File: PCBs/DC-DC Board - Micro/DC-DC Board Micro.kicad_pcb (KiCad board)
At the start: 2 copper layers, 58.4 x 36.8 mm, 56 parts, among them J1 Conn_01x01, J2 Conn_01x01, J3 Conn_01x02, J4 Conn_01x03, J5 Conn_01x01, J6 Conn_01x01, J7 USB_B_Mini, J8 Conn_02x05_Odd_Even, Q1 Q_NMOS_GDS, SW1 SW_Push, U1 ACS711, U2 DBQ0135V2, U3 TLV733P, U4 ATSAMD21E16L-MFT, Y1 32.7680kHz

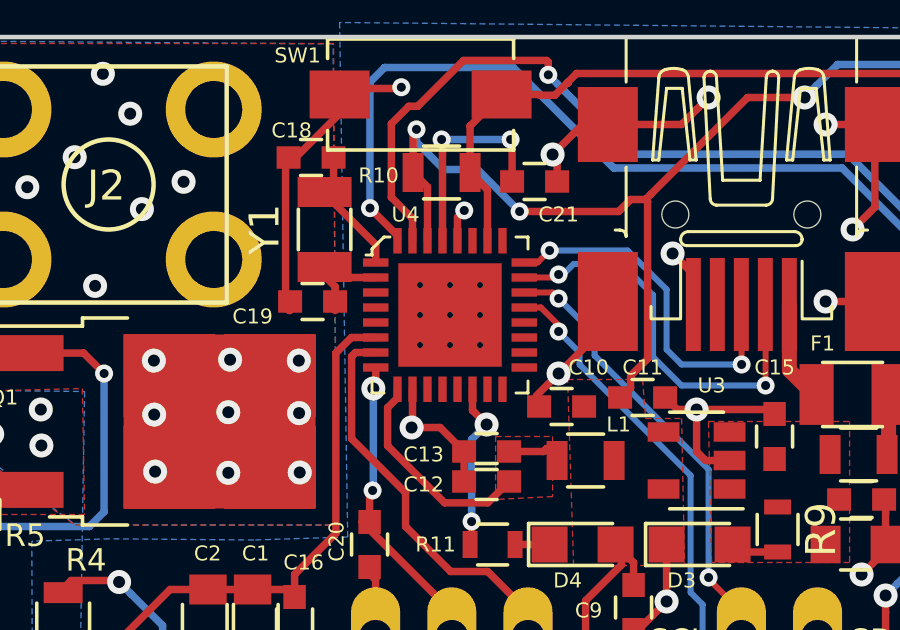
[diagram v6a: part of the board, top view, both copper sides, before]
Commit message: Minor Updates
Trying to sneak these Power PCBs through PCBWay, they caught me on a few 0.2mm drills so I made em 0.3. We'll see if my 0.2mm clearance passes their 8mil clearance (0.2035mm)
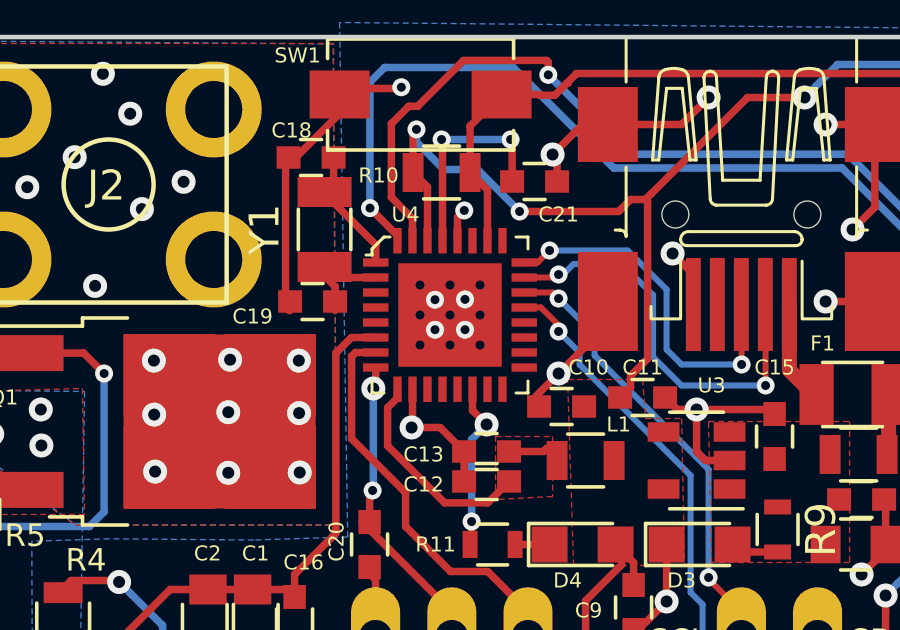
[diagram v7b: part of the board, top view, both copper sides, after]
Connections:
- U4 pad 33: (no net) -> GND
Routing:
- net GND: vias 35 -> 39
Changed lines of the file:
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@@
     (thickness 1.6)
     (drawings 24)
-    (tracks 512)
+    (tracks 516)
     (zones 0)
     (modules 56)
@@
     (last_trace_width 0.25)
     (trace_clearance 0.2)
-    (zone_clearance 0.25)
+    (zone_clearance 0.21)
     (zone_45_only no)
     (trace_min 0.2)
@@
     (uvia_drill 0.1)
     (uvias_allowed no)
-    (uvia_min_size 0.2)
+    (uvia_min_size 0.3)
     (uvia_min_drill 0.1)
     (pcb_text_width 0.3)
@@
     (visible_elements 7FFFFFFF)
     (pcbplotparams
-      (layerselection 0x010fc_ffffffff)
-      (usegerberextensions false)
+      (layerselection 0x010f0_ffffffff)
+      (usegerberextensions true)
       (usegerberattributes false)
       (usegerberadvancedattributes false)
@@
       (padsonsilk false)
       (subtractmaskfromsilk false)
-      (outputformat 4)
-      (mirror true)
+      (outputformat 1)
+      (mirror false)
       (drillshape 0)
       (scaleselection 1)
-      (outputdirectory ""))
+      (outputdirectory "Gerbers/"))
   )
   (net 0 "")
@@
     (pad 1 smd rect (at -2.995 -2.2 270) (size 0.28 0.85) (layers F.Cu F.Paste F.Mask)
       (net 21 "Net-(C18-Pad1)") (solder_mask_margin 0.07))
-    (pad 33 thru_hole circle (at -1.52 0.55 270) (size 0.2 0.2) (drill 0.2) (layers *.Cu *.Mask)
+    (pad 33 thru_hole circle (at -1.52 0.55 270) (size 0.3 0.3) (drill 0.3) (layers *.Cu *.Mask)
       (solder_mask_margin 0.1))
-    (pad 33 thru_hole circle (at -1.52 -0.45 270) (size 0.2 0.2) (drill 0.2) (layers *.Cu *.Mask)
+    (pad 33 thru_hole circle (at -1.52 -0.45 270) (size 0.3 0.3) (drill 0.3) (layers *.Cu *.Mask)
       (solder_mask_margin 0.1))
-    (pad 33 thru_hole circle (at -1.52 -1.45 270) (size 0.2 0.2) (drill 0.2) (layers *.Cu *.Mask)
+    (pad 33 thru_hole circle (at -1.52 -1.45 270) (size 0.3 0.3) (drill 0.3) (layers *.Cu *.Mask)
       (solder_mask_margin 0.1))
-    (pad 33 thru_hole circle (at -0.52 0.55 270) (size 0.2 0.2) (drill 0.2) (layers *.Cu *.Mask)
+    (pad 33 thru_hole circle (at -0.52 0.55 270) (size 0.3 0.3) (drill 0.3) (layers *.Cu *.Mask)
       (solder_mask_margin 0.1))
-    (pad 33 thru_hole circle (at -0.52 -0.450001 270) (size 0.2 0.2) (drill 0.2) (layers *.Cu *.Mask)
+    (pad 33 thru_hole circle (at -0.52 -0.450001 270) (size 0.3 0.3) (drill 0.3) (layers *.Cu *.Mask)
       (solder_mask_margin 0.1))
-    (pad 33 thru_hole circle (at -0.52 -1.45 270) (size 0.2 0.2) (drill 0.2) (layers *.Cu *.Mask)
+    (pad 33 thru_hole circle (at -0.52 -1.45 270) (size 0.3 0.3) (drill 0.3) (layers *.Cu *.Mask)
       (solder_mask_margin 0.1))
-    (pad 33 thru_hole circle (at 0.48 0.55 270) (size 0.2 0.2) (drill 0.2) (layers *.Cu *.Mask)
+    (pad 33 thru_hole circle (at 0.48 0.55 270) (size 0.3 0.3) (drill 0.3) (layers *.Cu *.Mask)
       (solder_mask_margin 0.1))
-    (pad 33 thru_hole circle (at 0.48 -0.45 270) (size 0.2 0.2) (drill 0.2) (layers *.Cu *.Mask)
+    (pad 33 thru_hole circle (at 0.48 -0.45 270) (size 0.3 0.3) (drill 0.3) (layers *.Cu *.Mask)
       (solder_mask_margin 0.1))
-    (pad 33 thru_hole circle (at 0.48 -1.45 270) (size 0.2 0.2) (drill 0.2) (layers *.Cu *.Mask)
+    (pad 33 thru_hole circle (at 0.48 -1.45 270) (size 0.3 0.3) (drill 0.3) (layers *.Cu *.Mask)
       (solder_mask_margin 0.1))
-    (pad 33 smd rect (at -0.52 -0.450001 270) (size 3.45 3.45) (layers F.Cu F.Paste F.Mask))
+    (pad 33 smd rect (at -0.52 -0.450001 270) (size 3.45 3.45) (layers F.Cu F.Paste F.Mask)
+      (net 3 GND))
     (pad 9 smd rect (at -2.27 2.025 270) (size 0.85 0.28) (layers F.Cu F.Paste F.Mask)
       (net 20 3V3_FILT) (solder_mask_margin 0.07))
@@
   (gr_line (start 129.2 33.585) (end 129.2 66.415) (layer Edge.Cuts) (width 0.15))
   (gr_line (start 72.8 31.585) (end 127.2 31.585) (layer Edge.Cuts) (width 0.15))
+  (via (at 90.88 40.34) (size 0.6) (drill 0.3) (layers F.Cu B.Cu) (net 3))
   (via (at 81.1 58.2) (size 0.6) (drill 0.3) (layers F.Cu B.Cu) (net 1))
   (via (at 82.7 57.3) (size 0.6) (drill 0.3) (layers F.Cu B.Cu) (net 1))
@@
   (segment (start 105.9 47.45) (end 105.9 48.5) (width 0.25) (layer F.Cu) (net 3))
   (segment (start 105.9 47) (end 105.9 47.45) (width 0.25) (layer F.Cu) (net 3))
+  (via (at 91.88 40.33) (size 0.6) (drill 0.3) (layers F.Cu B.Cu) (net 3))
+  (via (at 91.88 41.34) (size 0.6) (drill 0.3) (layers F.Cu B.Cu) (net 3))
+  (via (at 90.88 41.34) (size 0.6) (drill 0.3) (layers F.Cu B.Cu) (net 3))
   (segment (start 74.35 52.6) (end 73.9 52.6) (width 0.25) (layer F.Cu) (net 4))
   (via (at 72.75 51.45) (size 0.8) (drill 0.4) (layers F.Cu B.Cu) (net 4))
@@
   (zone (net 3) (net_name GND) (layer B.Cu) (hatch edge 0.508)
     (priority 1)
-    (connect_pads (clearance 0.25))
+    (connect_pads (clearance 0.21))
     (min_thickness 0.254)
     (fill yes (arc_segments 16) (thermal_gap 0.2) (thermal_bridge_width 1) (smoothing fillet) (radius 2))
